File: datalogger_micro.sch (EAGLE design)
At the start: 30 parts, among them IC1 DS3231/SO, IC2 MEGA8-P, Q1 8/16/20MHz, U2 MIC5205

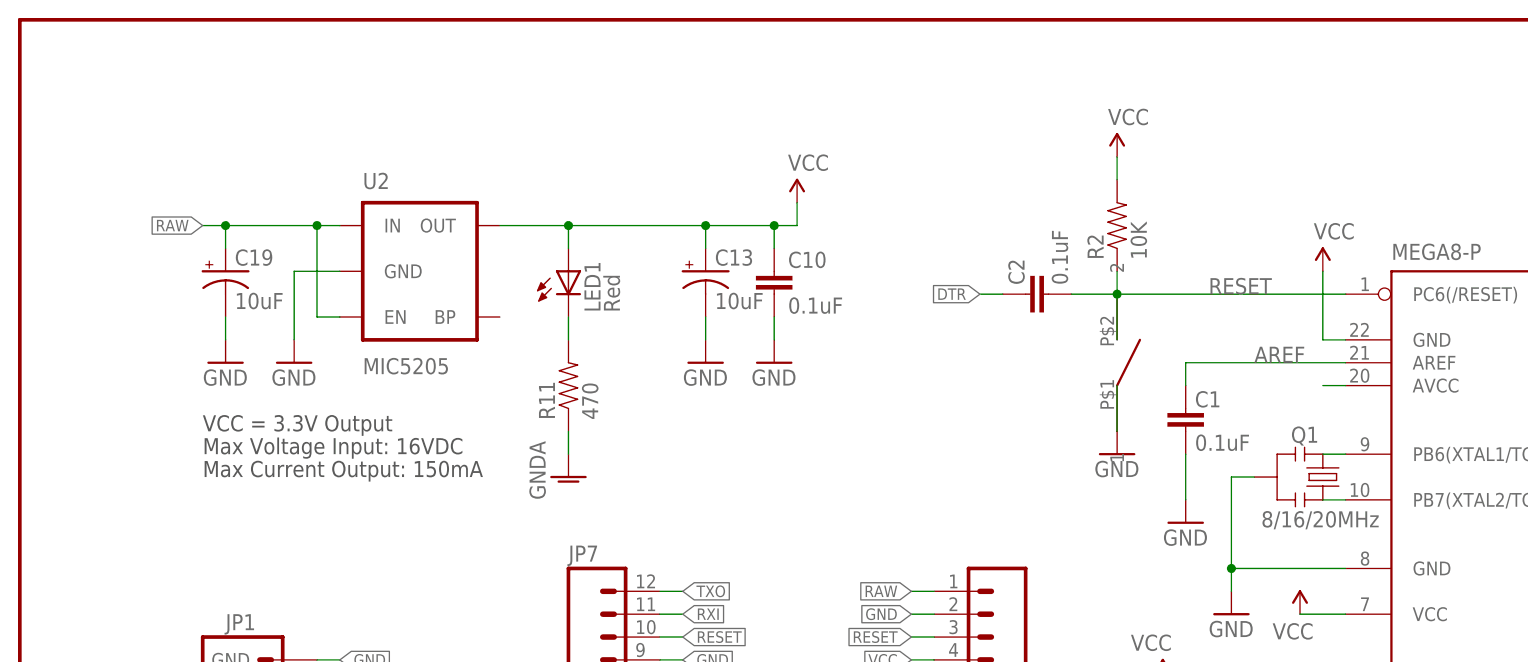
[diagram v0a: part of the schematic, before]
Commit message: version 0.94
first draft of 0.94, not the printed one.
integrates the LD117 voltage regulator
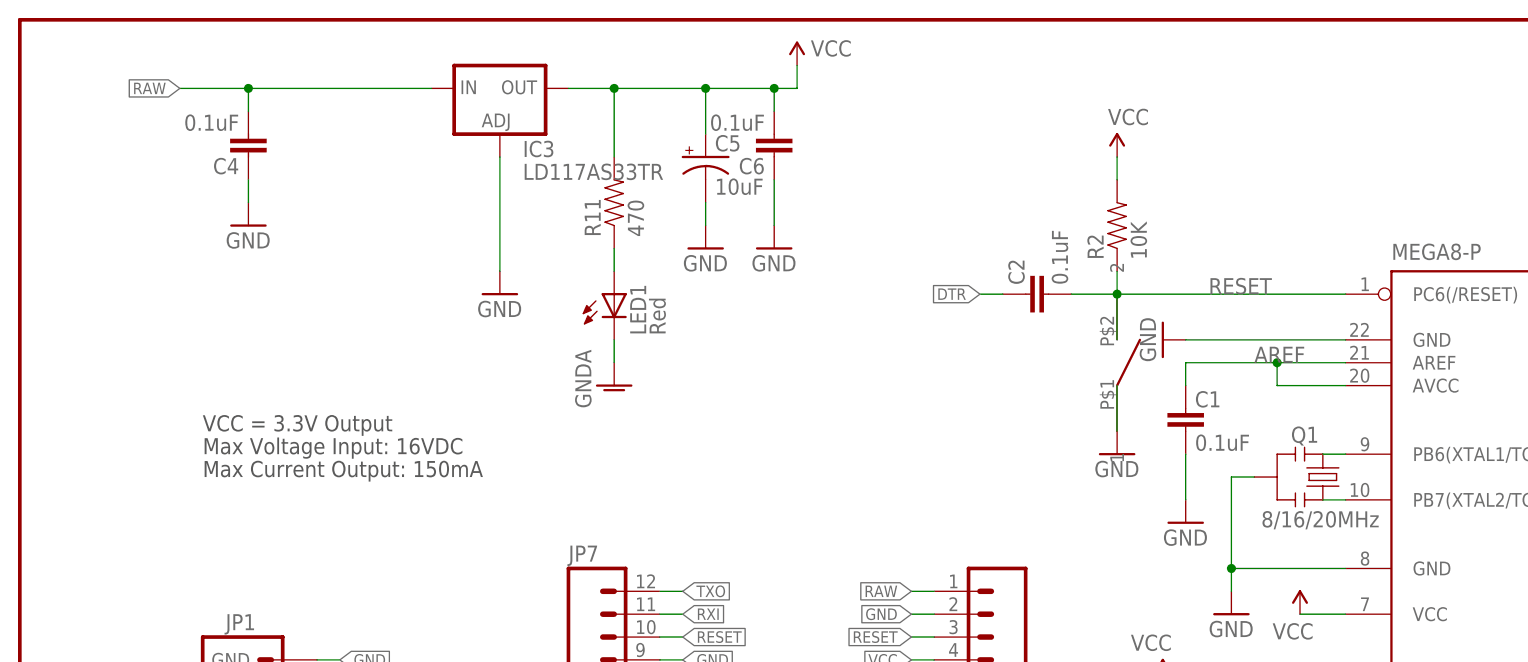
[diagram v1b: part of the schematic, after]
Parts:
- removed C10: 0.1uF, SparkFun:CAP0603-CAP
- removed C13, C19: 10uF, SparkFun:CAP_POL1206
- removed U2: MIC5205, SparkFun:V_REG_LDOSMD
- added C4, C6: 0.1uF, SparkFun:CAP0603-CAP
- added C5: 10uF, rcl:CPOL-USE2.5-5
- added IC3: LD117AS33TR, v-reg:LD117AS33TR
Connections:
- removed net N$3: IC2.AVCC
- net AREF: now also IC2.AVCC
- net GND: now also C4.2, C5.-, C6.2, IC2.GND, IC3.ADJ; no longer C10.2, C13.-, C19.-, U2.GND
- net GNDA: now also LED1.C; no longer R11.1
- net N$4: now also LED1.A, R11.1; no longer LED1.C, R11.2
- net RAW: now also C4.1, IC3.IN; no longer C19.+, U2.EN, U2.IN
- net VCC: now also C5.+, C6.1, IC3.OUT, R11.2; no longer C10.1, C13.+, IC2.GND, LED1.A, U2.OUT
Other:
- moved on the sheet: LED1, R11

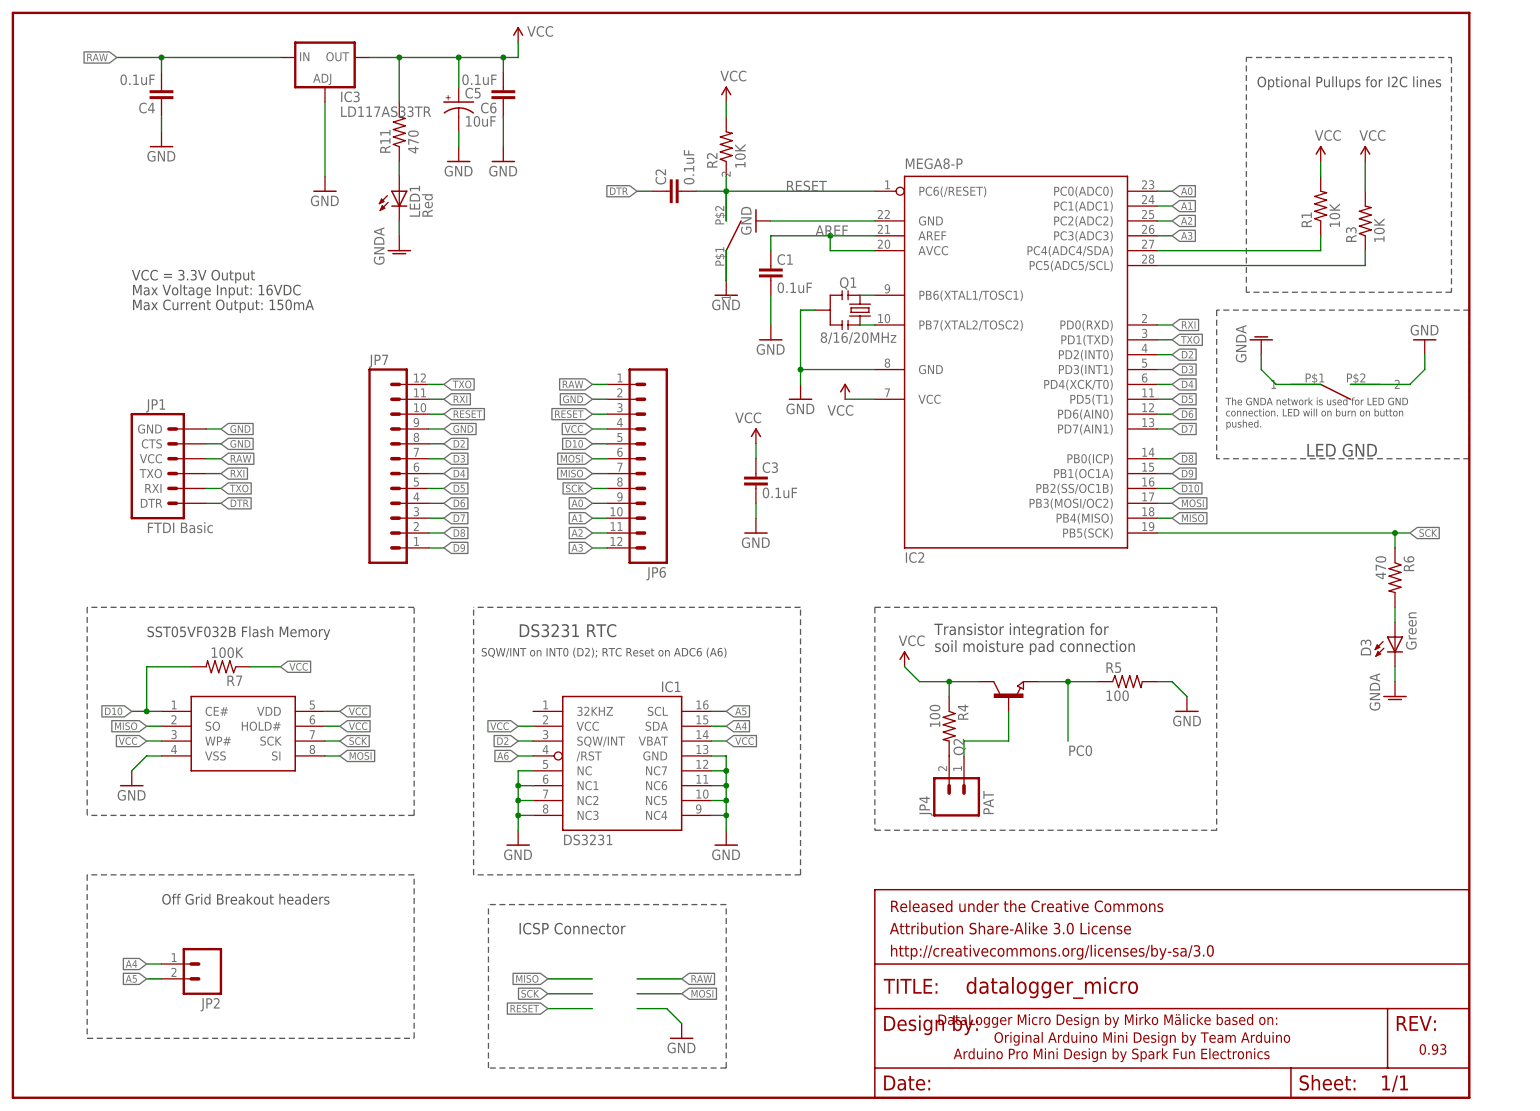
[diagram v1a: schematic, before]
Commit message: schematic rework for 0.95
Schematic rework for 0.95 version. Not productive, no layout.
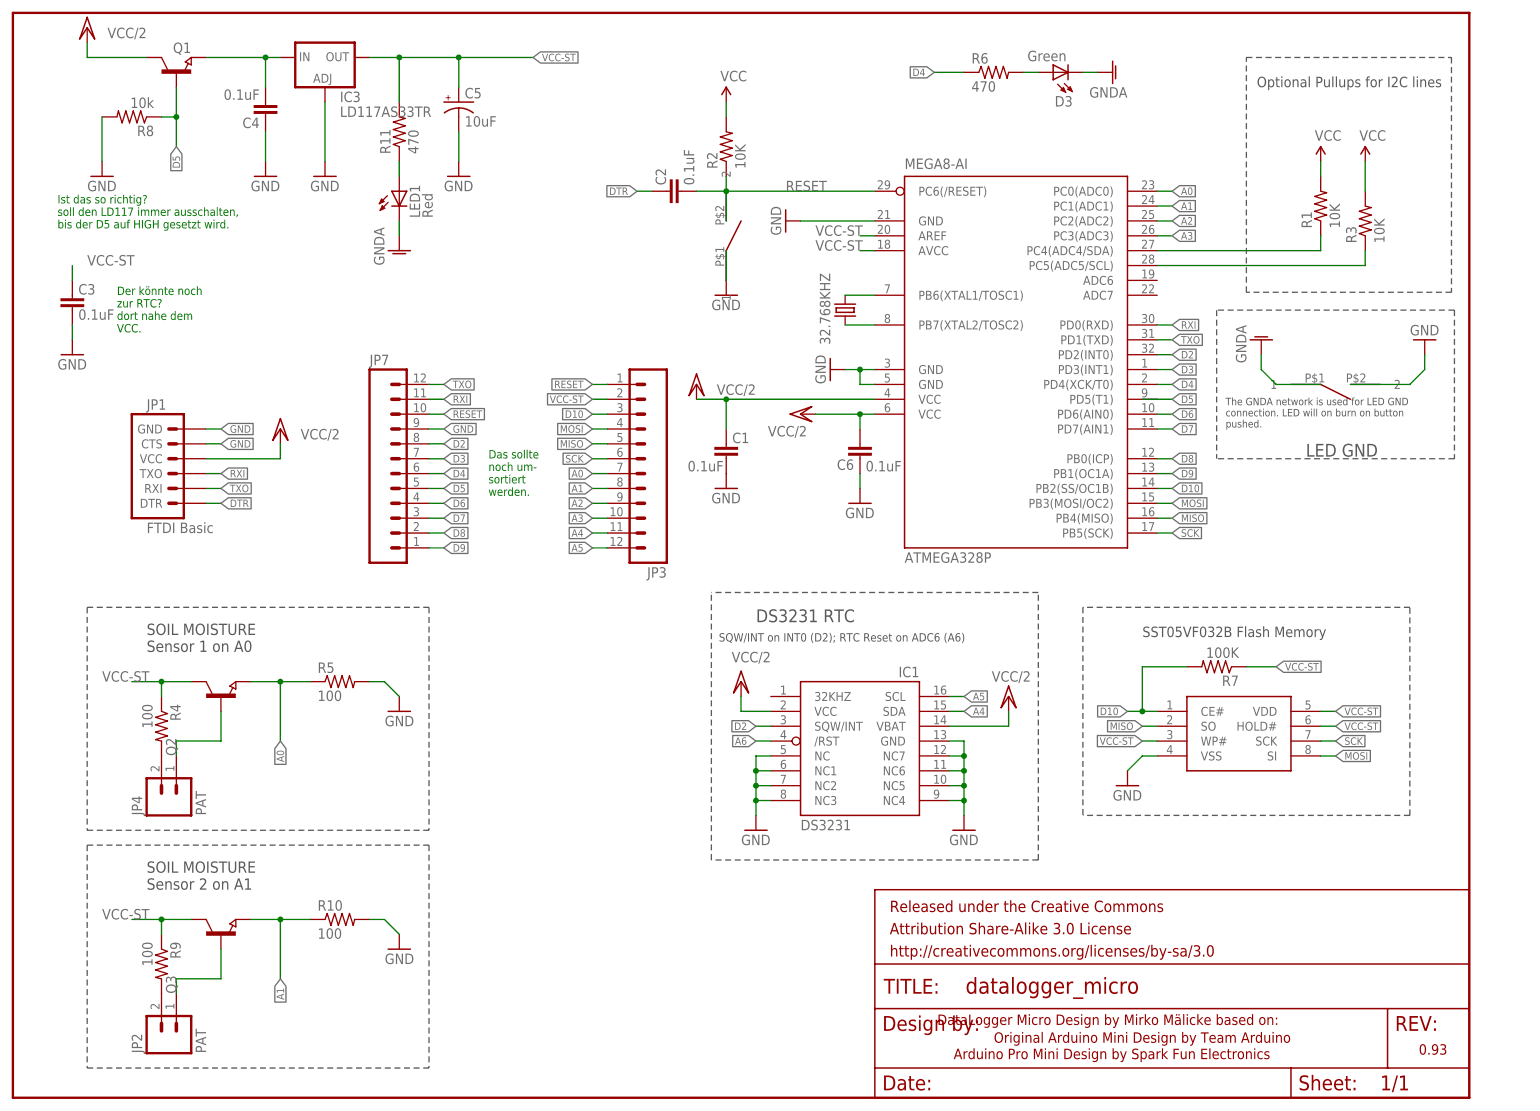
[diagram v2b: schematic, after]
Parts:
- removed IC2: MEGA8-P, atmel:MEGA8-P
- added 32.768KHZ: (no value), crystal:CRYSTALTC38H
- added ATMEGA328P: MEGA8-AI, atmel:MEGA8-AI
- added Q3: (no value), semicon-smd-ipc:NPN-TRANSISTOR_SOT23
- added R10, R9: 100, SparkFun:RESISTOR0603-RES
- added R8: 10k, SparkFun:RESISTOR0603-RES
- JP2: value (none) -> PAT
- Q1: value 8/16/20MHz -> (none); device Testing:RESONATOR1:1 -> semicon-smd-ipc:NPN-TRANSISTOR_SOT23
- renumbered JP6 to JP3
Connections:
- removed net 3.3V: IC2.VCC@1
- removed net AREF: C1.2, IC2.AREF, IC2.AVCC
- removed net RAW: C4.1, IC3.IN, JP1.VCC, JP3.1
- removed net VCC: C3.2, C5.+, C6.1, IC1.VBAT, IC1.VCC, IC3.OUT, JP3.4, Q2.C, R1.2, R11.2, R2.2, R3.2, R4.1, R7.1, U$2.HOLD#, U$2.VDD, U$2.WP#
- new net N$3: 32.768KHZ.2, ATMEGA328P.PB7(XTAL2/TOSC2)
- new net N$5: JP2.1, Q3.B
- new net N$8: JP2.2, R9.2
- new net VCC-ST: ATMEGA328P.AREF, ATMEGA328P.AVCC, C3.2, C5.+, IC3.OUT, JP3.2, Q2.C, Q3.C, R1.2, R11.2, R2.2, R3.2, R4.1, R7.1, R9.1, U$2.HOLD#, U$2.VDD, U$2.WP#
- new net VCC/2: ATMEGA328P.VCC@1, ATMEGA328P.VCC@2, C1.2, C6.1, IC1.VBAT, IC1.VCC, JP1.VCC, Q1.C
- net A0: now also ATMEGA328P.PC0(ADC0), JP3.7; no longer IC2.PC0(ADC0), JP3.9
- net A1: now also ATMEGA328P.PC1(ADC1), JP3.8, Q3.E, R10.1; no longer IC2.PC1(ADC1), JP3.10
- net A2: now also ATMEGA328P.PC2(ADC2), JP3.9; no longer IC2.PC2(ADC2), JP3.11
- net A3: now also ATMEGA328P.PC3(ADC3), JP3.10; no longer IC2.PC3(ADC3), JP3.12
- net A4: now also ATMEGA328P.PC4(ADC4/SDA), JP3.11; no longer IC2.PC4(ADC4/SDA), JP2.1
- net A5: now also ATMEGA328P.PC5(ADC5/SCL), JP3.12; no longer IC2.PC5(ADC5/SCL), JP2.2
- net D10: now also ATMEGA328P.PB2(SS/OC1B), JP3.3; no longer IC2.PB2(SS/OC1B), JP3.5
- net D2: now also ATMEGA328P.PD2(INT0); no longer IC2.PD2(INT0)
- net D3: now also ATMEGA328P.PD3(INT1); no longer IC2.PD3(INT1)
- net D4: now also ATMEGA328P.PD4(XCK/T0), R6.1; no longer IC2.PD4(XCK/T0)
- net D5: now also ATMEGA328P.PD5(T1), Q1.B, R8.1; no longer IC2.PD5(T1)
- net D6: now also ATMEGA328P.PD6(AIN0); no longer IC2.PD6(AIN0)
- net D7: now also ATMEGA328P.PD7(AIN1); no longer IC2.PD7(AIN1)
- net D8: now also ATMEGA328P.PB0(ICP); no longer IC2.PB0(ICP)
- net D9: now also ATMEGA328P.PB1(OC1A); no longer IC2.PB1(OC1A)
- net GND: now also ATMEGA328P.GND, ATMEGA328P.GND@1, ATMEGA328P.GND@2, R10.2, R8.2; no longer IC2.GND, IC2.GND@1, JP3.2, Q1.2
- net MISO: now also ATMEGA328P.PB4(MISO), JP3.5; no longer IC2.PB4(MISO), JP3.7
- net MOSI: now also ATMEGA328P.PB3(MOSI/OC2), JP3.4; no longer IC2.PB3(MOSI/OC2), JP3.6
- net N$1: now also C4.1, IC3.IN, Q1.E; no longer IC2.PB6(XTAL1/TOSC1), Q1.1
- net N$2: now also 32.768KHZ.1, ATMEGA328P.PB6(XTAL1/TOSC1); no longer IC2.PB7(XTAL2/TOSC2), Q1.3
- net RESET: now also ATMEGA328P.PC6(/RESET), JP3.1; no longer IC2.PC6(/RESET), JP3.3
- net RXI: now also ATMEGA328P.PD0(RXD); no longer IC2.PD0(RXD)
- net SCK: now also ATMEGA328P.PB5(SCK), JP3.6; no longer IC2.PB5(SCK), JP3.8, R6.1
- net TXO: now also ATMEGA328P.PD1(TXD); no longer IC2.PD1(TXD)
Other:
- note added: "Das sollte noch um- sortiert werden."
- note added: "Der könnte noch zur RTC? dort nahe dem VCC."
- note added: "Ist das so richtig? soll den LD117 immer ausschalten, bis der D5 auf HIGH gesetzt wird."
- note added: "SOIL MOISTURE Sensor 1 on A0"
- note added: "SOIL MOISTURE Sensor 2 on A1"
- note removed: "ICSP Connector"
- note removed: "Max Current Output: 150mA"
- note removed: "Max Voltage Input: 16VDC"
- note removed: "Off Grid Breakout headers"
- note removed: "Transistor integration for soil moisture pad connection"
- note removed: "VCC = 3.3V Output"
- moved on the sheet: C1, C3, C4, C6, D3, IC1, JP2, JP4, Q2, R4, R5, R6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

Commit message: layout rework
Still need to include the battery, maybe replace LM117
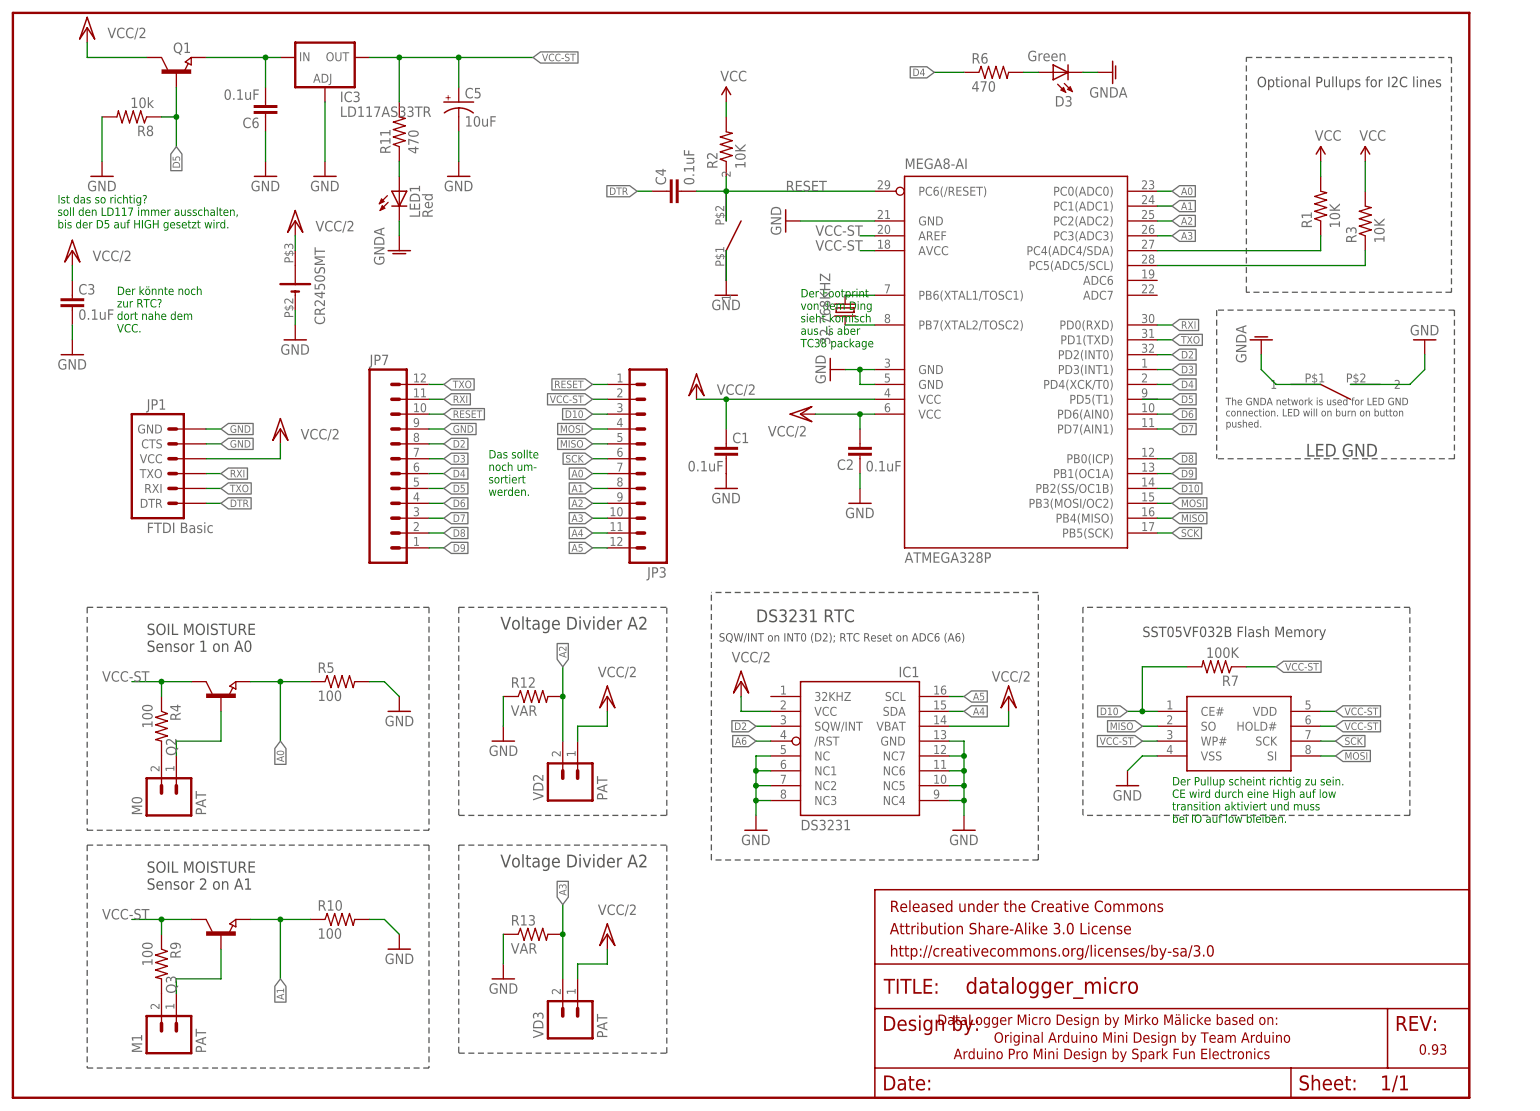
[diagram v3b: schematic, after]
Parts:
- added R12, R13: VAR, SparkFun:RESISTOR0603-RES
- added U$3: CR2450SMT, battery:CR2450SMT
- added VD2, VD3: PAT, SparkFun:M02PTH
- renumbered JP2 to M1, JP4 to M0
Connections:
- net A2: now also R12.2, VD2.2
- net A3: now also R13.2, VD3.2
- net DTR: now also C4.2; no longer C2.2
- net GND: now also C2.2, R12.1, R13.1, U$3.-; no longer C4.2
- net N$1: now also C6.1; no longer C4.1
- net RESET: now also C4.1; no longer C2.1
- net VCC-ST: no longer C3.2
- net VCC/2: now also C2.1, C3.2, U$3.+, VD2.1, VD3.1; no longer C6.1
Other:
- note added: "Der Footprint von dem Ding sieht komisch aus. Is aber TC38 package"
- note added: "Der Pullup scheint richtig zu sein. CE wird durch eine High auf low transition aktiviert und muss bei IO auf low bleiben."
- note added: "Voltage Divider A2"
- moved on the sheet: C2, C4, C6

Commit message: same as last
another variant of LIR2450
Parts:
- added G1: CR2450V, battery:CR2450V
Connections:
- net GND: now also G1.-
- net VCC/2: now also G1.+
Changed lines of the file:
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@@
 <part name="GND18" library="SparkFun" deviceset="GND" device=""/>
 <part name="U$3" library="battery" deviceset="CR2450SMT" device=""/>
+<part name="G1" library="battery" deviceset="CR2450V" device=""/>
+<part name="VCC-BAT8" library="supply1" deviceset="VCC/2" device=""/>
+<part name="GND19" library="SparkFun" deviceset="GND" device=""/>
 </parts>
 <sheets>
@@
 <attribute name="VALUE" x="20.32" y="144.78" size="1.778" layer="96" rot="R180"/>
 </instance>
-<instance part="VCC-BAT7" gate="G$1" x="48.26" y="149.86" smashed="yes">
-<attribute name="VALUE" x="58.42" y="149.86" size="1.778" layer="96" rot="R180"/>
-</instance>
-<instance part="GND18" gate="1" x="48.26" y="129.54"/>
-<instance part="U$3" gate="G$1" x="48.26" y="139.7" smashed="yes" rot="R90">
-<attribute name="VALUE" x="53.34" y="132.08" size="1.778" layer="96" rot="R90"/>
-</instance>
+<instance part="VCC-BAT7" gate="G$1" x="81.28" y="149.86" smashed="yes">
+<attribute name="VALUE" x="91.44" y="149.86" size="1.778" layer="96" rot="R180"/>
+</instance>
+<instance part="GND18" gate="1" x="81.28" y="129.54"/>
+<instance part="U$3" gate="G$1" x="81.28" y="139.7" smashed="yes" rot="R90">
+<attribute name="VALUE" x="86.36" y="132.08" size="1.778" layer="96" rot="R90"/>
+</instance>
+<instance part="G1" gate="1" x="96.52" y="139.7" rot="R90"/>
+<instance part="VCC-BAT8" gate="G$1" x="96.52" y="149.86" smashed="yes">
+<attribute name="VALUE" x="106.68" y="149.86" size="1.778" layer="96" rot="R180"/>
+</instance>
+<instance part="GND19" gate="1" x="96.52" y="129.54"/>
 </instances>
 <busses>
@@
 <segment>
 <pinref part="GND18" gate="1" pin="GND"/>
-<wire x1="48.26" y1="132.08" x2="48.26" y2="134.62" width="0.1524" layer="91"/>
+<wire x1="81.28" y1="132.08" x2="81.28" y2="134.62" width="0.1524" layer="91"/>
 <pinref part="U$3" gate="G$1" pin="-"/>
+</segment>
+<segment>
+<pinref part="GND19" gate="1" pin="GND"/>
+<pinref part="G1" gate="1" pin="-"/>
+<wire x1="96.52" y1="132.08" x2="96.52" y2="134.62" width="0.1524" layer="91"/>
 </segment>
 </net>
@@
 <segment>
 <pinref part="VCC-BAT7" gate="G$1" pin="VCC/2"/>
-<wire x1="48.26" y1="144.78" x2="48.26" y2="147.32" width="0.1524" layer="91"/>
+<wire x1="81.28" y1="144.78" x2="81.28" y2="147.32" width="0.1524" layer="91"/>
 <pinref part="U$3" gate="G$1" pin="+"/>
 </segment>
-</net>
+<segment>
+<pinref part="G1" gate="1" pin="+"/>
+<pinref part="VCC-BAT8" gate="G$1" pin="VCC/2"/>
+<wire x1="96.52" y1="144.78" x2="96.52" y2="147.32" width="0.1524" layer="91"/>
+</segment>
+</net>
